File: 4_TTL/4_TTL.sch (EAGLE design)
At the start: 3 parts, among them J1 MA03-2W, X1 ALLSERIALD, X2 AKL18X-10W

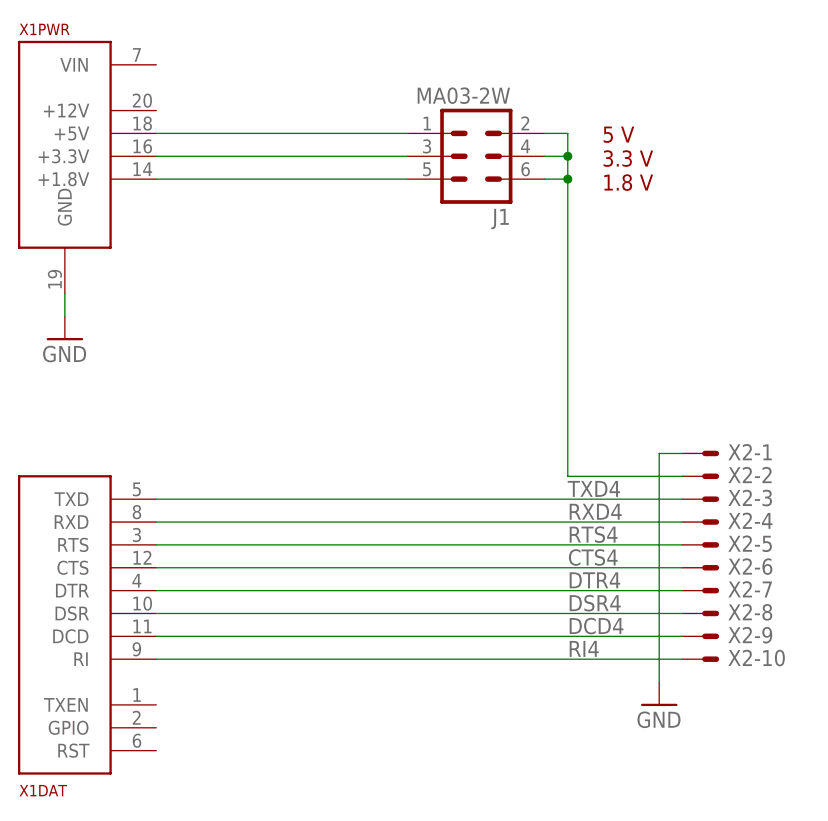
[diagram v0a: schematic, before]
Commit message: insert diode for supply
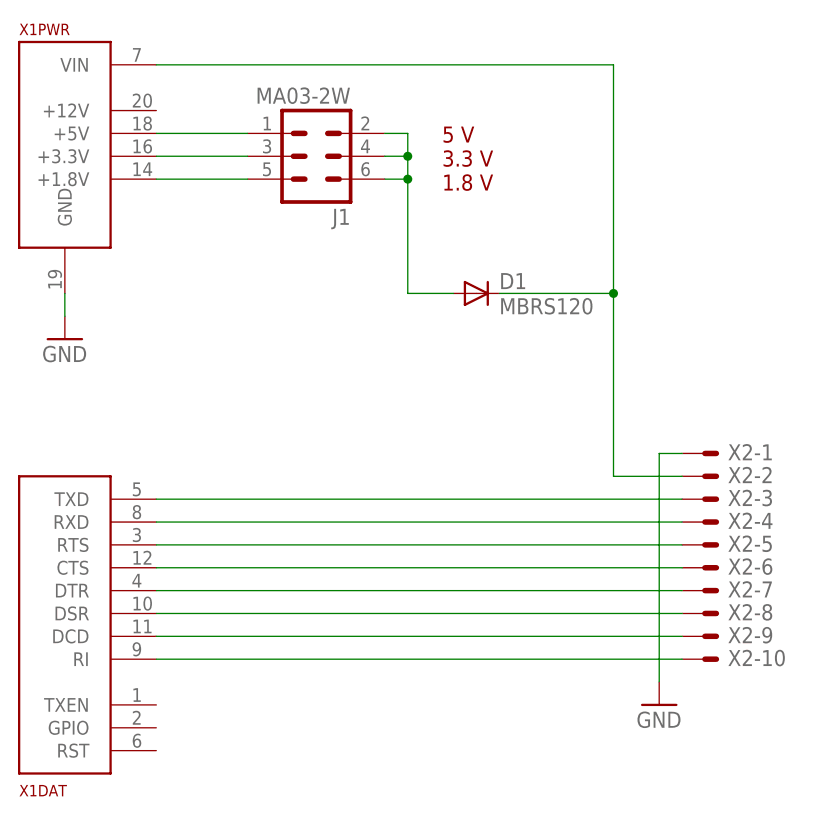
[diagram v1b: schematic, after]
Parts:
- added D1: MBRS120, diode:DIODE-DO214AA
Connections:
- new net N$5: D1.C, X1PWR.VIN, X2-2.S
- net N$1: now also D1.A; no longer X2-2.S
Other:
- moved on the sheet: J1
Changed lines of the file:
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@@
 <?xml version="1.0" encoding="utf-8"?>
 <!DOCTYPE eagle SYSTEM "eagle.dtd">
-<eagle version="7.7.0">
+<eagle version="7.6.0">
 <drawing>
 <settings>
@@
 <part name="GND2" library="supply1" deviceset="GND" device=""/>
 <part name="J1" library="con-lstb" deviceset="MA03-2W" device=""/>
+<part name="D1" library="diode" deviceset="DIODE-" device="DO214AA" value="MBRS120"/>
 </parts>
 <sheets>
 <sheet>
 <plain>
-<text x="105.41" y="115.57" size="1.778" layer="94">5 V
+<text x="87.63" y="115.57" size="1.778" layer="94">5 V
 3.3 V
 1.8 V</text>
@@
 <instance part="GND1" gate="1" x="45.72" y="99.06"/>
 <instance part="GND2" gate="1" x="111.76" y="58.42"/>
-<instance part="J1" gate="G$1" x="91.44" y="119.38" rot="R180"/>
+<instance part="J1" gate="G$1" x="73.66" y="119.38" rot="R180"/>
+<instance part="D1" gate="G$1" x="91.44" y="104.14"/>
 </instances>
 <busses>
@@
 <segment>
 <pinref part="X2" gate="-3" pin="S"/>
-<label x="101.6" y="81.534" size="1.778" layer="95"/>
 <pinref part="X1" gate="DAT" pin="TXD"/>
 <wire x1="114.3" y1="81.28" x2="55.88" y2="81.28" width="0.1524" layer="91"/>
@@
 <segment>
 <pinref part="X2" gate="-4" pin="S"/>
-<label x="101.6" y="78.994" size="1.778" layer="95"/>
 <pinref part="X1" gate="DAT" pin="RXD"/>
 <wire x1="114.3" y1="78.74" x2="55.88" y2="78.74" width="0.1524" layer="91"/>
@@
 <segment>
 <pinref part="X2" gate="-5" pin="S"/>
-<label x="101.6" y="76.454" size="1.778" layer="95"/>
 <pinref part="X1" gate="DAT" pin="RTS"/>
 <wire x1="55.88" y1="76.2" x2="114.3" y2="76.2" width="0.1524" layer="91"/>
@@
 <segment>
 <pinref part="X2" gate="-6" pin="S"/>
-<label x="101.6" y="73.914" size="1.778" layer="95"/>
 <pinref part="X1" gate="DAT" pin="CTS"/>
 <wire x1="114.3" y1="73.66" x2="55.88" y2="73.66" width="0.1524" layer="91"/>
@@
 <segment>
 <pinref part="X2" gate="-7" pin="S"/>
-<label x="101.6" y="71.374" size="1.778" layer="95"/>
 <pinref part="X1" gate="DAT" pin="DTR"/>
 <wire x1="114.3" y1="71.12" x2="55.88" y2="71.12" width="0.1524" layer="91"/>
@@
 <segment>
 <pinref part="X2" gate="-8" pin="S"/>
-<label x="101.6" y="68.834" size="1.778" layer="95"/>
 <pinref part="X1" gate="DAT" pin="DSR"/>
 <wire x1="114.3" y1="68.58" x2="55.88" y2="68.58" width="0.1524" layer="91"/>
@@
 <segment>
 <pinref part="X2" gate="-9" pin="S"/>
-<label x="101.6" y="66.294" size="1.778" layer="95"/>
 <pinref part="X1" gate="DAT" pin="DCD"/>
 <wire x1="55.88" y1="66.04" x2="114.3" y2="66.04" width="0.1524" layer="91"/>
@@
 <segment>
 <pinref part="X2" gate="-10" pin="S"/>
-<label x="101.6" y="63.754" size="1.778" layer="95"/>
 <pinref part="X1" gate="DAT" pin="RI"/>
 <wire x1="114.3" y1="63.5" x2="55.88" y2="63.5" width="0.1524" layer="91"/>
@@
 <net name="N$1" class="0">
 <segment>
-<pinref part="X2" gate="-2" pin="S"/>
-<wire x1="114.3" y1="83.82" x2="101.6" y2="83.82" width="0.1524" layer="91"/>
-<wire x1="101.6" y1="83.82" x2="101.6" y2="116.84" width="0.1524" layer="91"/>
 <pinref part="J1" gate="G$1" pin="2"/>
-<wire x1="101.6" y1="116.84" x2="101.6" y2="119.38" width="0.1524" layer="91"/>
-<wire x1="101.6" y1="119.38" x2="101.6" y2="121.92" width="0.1524" layer="91"/>
-<wire x1="101.6" y1="121.92" x2="99.06" y2="121.92" width="0.1524" layer="91"/>
+<wire x1="83.82" y1="116.84" x2="83.82" y2="119.38" width="0.1524" layer="91"/>
+<wire x1="83.82" y1="119.38" x2="83.82" y2="121.92" width="0.1524" layer="91"/>
+<wire x1="83.82" y1="121.92" x2="81.28" y2="121.92" width="0.1524" layer="91"/>
 <pinref part="J1" gate="G$1" pin="4"/>
-<wire x1="99.06" y1="119.38" x2="101.6" y2="119.38" width="0.1524" layer="91"/>
-<junction x="101.6" y="119.38"/>
+<wire x1="81.28" y1="119.38" x2="83.82" y2="119.38" width="0.1524" layer="91"/>
+<junction x="83.82" y="119.38"/>
 <pinref part="J1" gate="G$1" pin="6"/>
-<wire x1="99.06" y1="116.84" x2="101.6" y2="116.84" width="0.1524" layer="91"/>
-<junction x="101.6" y="116.84"/>
+<wire x1="81.28" y1="116.84" x2="83.82" y2="116.84" width="0.1524" layer="91"/>
+<pinref part="D1" gate="G$1" pin="A"/>
+<wire x1="88.9" y1="104.14" x2="83.82" y2="104.14" width="0.1524" layer="91"/>
+<wire x1="83.82" y1="104.14" x2="83.82" y2="116.84" width="0.1524" layer="91"/>
+<junction x="83.82" y="116.84"/>
 </segment>
 </net>
@@
 <pinref part="X1" gate="PWR" pin="+1.8V"/>
 <pinref part="J1" gate="G$1" pin="5"/>
-<wire x1="55.88" y1="116.84" x2="83.82" y2="116.84" width="0.1524" layer="91"/>
+<wire x1="55.88" y1="116.84" x2="66.04" y2="116.84" width="0.1524" layer="91"/>
 </segment>
 </net>
@@
 <pinref part="X1" gate="PWR" pin="+3.3V"/>
 <pinref part="J1" gate="G$1" pin="3"/>
-<wire x1="55.88" y1="119.38" x2="83.82" y2="119.38" width="0.1524" layer="91"/>
+<wire x1="55.88" y1="119.38" x2="66.04" y2="119.38" width="0.1524" layer="91"/>
 </segment>
 </net>
@@
 <pinref part="X1" gate="PWR" pin="+5V"/>
 <pinref part="J1" gate="G$1" pin="1"/>
-<wire x1="55.88" y1="121.92" x2="83.82" y2="121.92" width="0.1524" layer="91"/>
-</segment>
-</net>
+<wire x1="55.88" y1="121.92" x2="66.04" y2="121.92" width="0.1524" layer="91"/>
+</segment>
+</net>
+<net name="N$5" class="0">
+<segment>
+<pinref part="X2" gate="-2" pin="S"/>
+<wire x1="114.3" y1="83.82" x2="106.68" y2="83.82" width="0.1524" layer="91"/>
+<pinref part="X1" gate="PWR" pin="VIN"/>
+<wire x1="55.88" y1="129.54" x2="106.68" y2="129.54" width="0.1524" layer="91"/>
+<wire x1="106.68" y1="129.54" x2="106.68" y2="104.14" width="0.1524" layer="91"/>
+<pinref part="D1" gate="G$1" pin="C"/>
+<wire x1="106.68" y1="104.14" x2="106.68" y2="83.82" width="0.1524" layer="91"/>
+<wire x1="93.98" y1="104.14" x2="106.68" y2="104.14" width="0.1524" layer="91"/>
+<junction x="106.68" y="104.14"/>
+</segment>
+</net>

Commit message: new BOMs,
finish TTY board
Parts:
- D1: OC_REICHELT (none) -> MBRS120SMD
- J1: OC_REICHELT (none) -> MPE 088-2-006
- X1: OC_REICHELT (none) -> SL 2X10W 2,54
- X2: OC_REICHELT (none) -> AKL 182-10
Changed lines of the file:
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@@
 <parts>
 <part name="FRAME4" library="frames" deviceset="A4L-LOC" device=""/>
-<part name="X2" library="con-riacon_akl" deviceset="AKL18X-10" device="W"/>
-<part name="X1" library="AllSerial" deviceset="ALLSERIAL" device="D"/>
+<part name="X2" library="con-riacon_akl" deviceset="AKL18X-10" device="W">
+<attribute name="OC_REICHELT" value="AKL 182-10"/>
+</part>
+<part name="X1" library="AllSerial" deviceset="ALLSERIAL" device="D">
+<attribute name="OC_REICHELT" value="SL 2X10W 2,54"/>
+</part>
 <part name="GND1" library="supply1" deviceset="GND" device=""/>
 <part name="GND2" library="supply1" deviceset="GND" device=""/>
-<part name="J1" library="con-lstb" deviceset="MA03-2W" device=""/>
-<part name="D1" library="diode" deviceset="DIODE-" device="DO214AA" value="MBRS120"/>
+<part name="J1" library="con-lstb" deviceset="MA03-2W" device="">
+<attribute name="OC_REICHELT" value="MPE 088-2-006"/>
+</part>
+<part name="D1" library="diode" deviceset="DIODE-" device="DO214AA" value="MBRS120">
+<attribute name="OC_REICHELT" value="MBRS120SMD"/>
+</part>
 </parts>
 <sheets>
@@
 <instance part="X2" gate="-3" x="116.84" y="81.28"/>
 <instance part="X2" gate="-4" x="116.84" y="78.74"/>
-<instance part="X2" gate="-5" x="116.84" y="76.2"/>
+<instance part="X2" gate="-5" x="116.84" y="76.2">
+<attribute name="OC_REICHELT" x="116.84" y="76.2" size="1.778" layer="96" display="off"/>
+</instance>
 <instance part="X2" gate="-6" x="116.84" y="73.66"/>
 <instance part="X2" gate="-7" x="116.84" y="71.12"/>
@@
 <instance part="X2" gate="-9" x="116.84" y="66.04"/>
 <instance part="X2" gate="-10" x="116.84" y="63.5"/>
-<instance part="X1" gate="DAT" x="45.72" y="66.04"/>
+<instance part="X1" gate="DAT" x="45.72" y="66.04">
+<attribute name="OC_REICHELT" x="45.72" y="66.04" size="1.778" layer="96" display="off"/>
+</instance>
 <instance part="X1" gate="PWR" x="45.72" y="119.38"/>
 <instance part="GND1" gate="1" x="45.72" y="99.06"/>
 <instance part="GND2" gate="1" x="111.76" y="58.42"/>
-<instance part="J1" gate="G$1" x="73.66" y="119.38" rot="R180"/>
-<instance part="D1" gate="G$1" x="91.44" y="104.14"/>
+<instance part="J1" gate="G$1" x="73.66" y="119.38" rot="R180">
+<attribute name="OC_REICHELT" x="73.66" y="119.38" size="1.778" layer="96" rot="R180" display="off"/>
+</instance>
+<instance part="D1" gate="G$1" x="91.44" y="104.14">
+<attribute name="OC_REICHELT" x="91.44" y="104.14" size="1.778" layer="96" display="off"/>
+</instance>
 </instances>
 <busses>

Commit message: add author
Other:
- note added: "Seegel Systeme Königstraße 57 90762 Fürth www.seegel-systeme.de post@seegel-systeme.de +49 (911) / 8915295"
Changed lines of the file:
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@@
 <?xml version="1.0" encoding="utf-8"?>
 <!DOCTYPE eagle SYSTEM "eagle.dtd">
-<eagle version="7.6.0">
+<eagle version="7.7.0">
 <drawing>
 <settings>
@@
 3.3 V
 1.8 V</text>
+<text x="165.1" y="7.62" size="1.778" layer="94">Seegel Systeme
+Königstraße 57
+90762 Fürth
+www.seegel-systeme.de
+post@seegel-systeme.de
++49 (911) / 8915295</text>
 </plain>
 <instances>

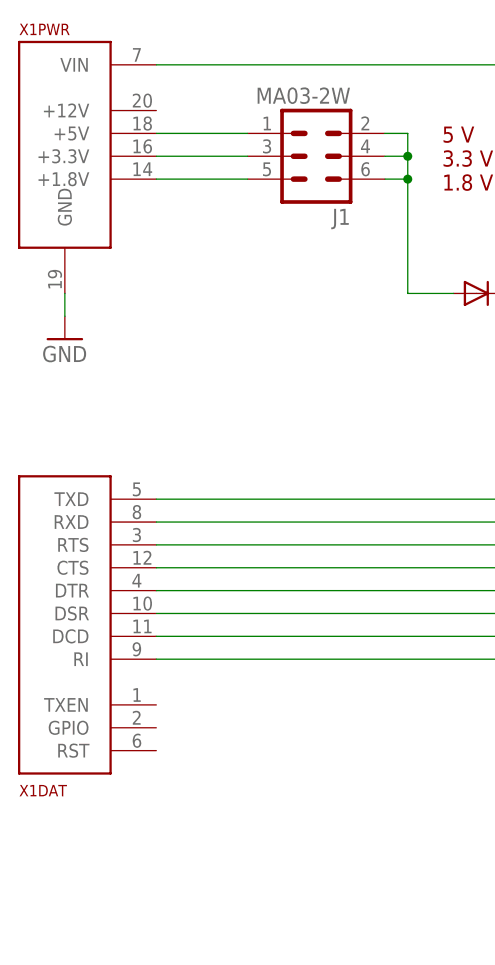
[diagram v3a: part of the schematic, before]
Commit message: change to libv2
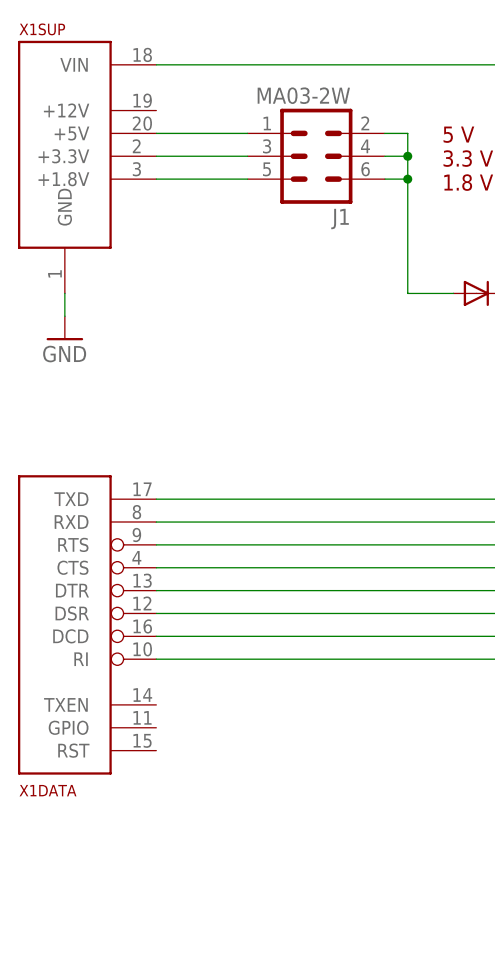
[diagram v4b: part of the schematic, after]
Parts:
- X1: value ALLSERIALD -> ALLSERIALSLAVE; device AllSerial:ALLSERIALD -> AllSerialv2:ALLSERIALSLAVE; OC_REICHELT SL 2X10W 2,54 -> (none)
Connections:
- net CTS4: now also X1DATA.CTS; no longer X1DAT.CTS
- net DCD4: now also X1DATA.DCD; no longer X1DAT.DCD
- net DSR4: now also X1DATA.DSR; no longer X1DAT.DSR
- net DTR4: now also X1DATA.DTR; no longer X1DAT.DTR
- net GND: now also X1SUP.GND; no longer X1PWR.GND
- net N$2: now also X1SUP.+1.8V; no longer X1PWR.+1.8V
- net N$3: now also X1SUP.+3.3V; no longer X1PWR.+3.3V
- net N$4: now also X1SUP.+5V; no longer X1PWR.+5V
- net N$5: now also X1SUP.VIN; no longer X1PWR.VIN
- net RI4: now also X1DATA.RI; no longer X1DAT.RI
- net RTS4: now also X1DATA.RTS; no longer X1DAT.RTS
- net RXD4: now also X1DATA.RXD; no longer X1DAT.RXD
- net TXD4: now also X1DATA.TXD; no longer X1DAT.TXD
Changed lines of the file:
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@@
 <?xml version="1.0" encoding="utf-8"?>
 <!DOCTYPE eagle SYSTEM "eagle.dtd">
-<eagle version="7.7.0">
+<eagle version="7.6.0">
 <drawing>
 <settings>
@@
 <attribute name="OC_REICHELT" value="AKL 182-10"/>
 </part>
-<part name="X1" library="AllSerial" deviceset="ALLSERIAL" device="D">
-<attribute name="OC_REICHELT" value="SL 2X10W 2,54"/>
-</part>
 <part name="GND1" library="supply1" deviceset="GND" device=""/>
 <part name="GND2" library="supply1" deviceset="GND" device=""/>
@@
 <attribute name="OC_REICHELT" value="MBRS120SMD"/>
 </part>
+<part name="X1" library="AllSerialv2" deviceset="ALLSERIALSLAVE" device=""/>
 </parts>
 <sheets>
@@
 <instance part="X2" gate="-9" x="116.84" y="66.04"/>
 <instance part="X2" gate="-10" x="116.84" y="63.5"/>
-<instance part="X1" gate="DAT" x="45.72" y="66.04">
-<attribute name="OC_REICHELT" x="45.72" y="66.04" size="1.778" layer="96" display="off"/>
-</instance>
-<instance part="X1" gate="PWR" x="45.72" y="119.38"/>
 <instance part="GND1" gate="1" x="45.72" y="99.06"/>
 <instance part="GND2" gate="1" x="111.76" y="58.42"/>
@@
 <attribute name="OC_REICHELT" x="91.44" y="104.14" size="1.778" layer="96" display="off"/>
 </instance>
+<instance part="X1" gate="DATA" x="45.72" y="66.04"/>
+<instance part="X1" gate="SUP" x="45.72" y="119.38"/>
 </instances>
 <busses>
@@
 <segment>
 <pinref part="X2" gate="-3" pin="S"/>
-<pinref part="X1" gate="DAT" pin="TXD"/>
 <wire x1="114.3" y1="81.28" x2="55.88" y2="81.28" width="0.1524" layer="91"/>
+<pinref part="X1" gate="DATA" pin="TXD"/>
 </segment>
 </net>
@@
 <segment>
 <pinref part="X2" gate="-4" pin="S"/>
-<pinref part="X1" gate="DAT" pin="RXD"/>
 <wire x1="114.3" y1="78.74" x2="55.88" y2="78.74" width="0.1524" layer="91"/>
+<pinref part="X1" gate="DATA" pin="RXD"/>
 </segment>
 </net>
@@
 <segment>
 <pinref part="X2" gate="-5" pin="S"/>
-<pinref part="X1" gate="DAT" pin="RTS"/>
 <wire x1="55.88" y1="76.2" x2="114.3" y2="76.2" width="0.1524" layer="91"/>
+<pinref part="X1" gate="DATA" pin="RTS"/>
 </segment>
 </net>
@@
 <segment>
 <pinref part="X2" gate="-6" pin="S"/>
-<pinref part="X1" gate="DAT" pin="CTS"/>
 <wire x1="114.3" y1="73.66" x2="55.88" y2="73.66" width="0.1524" layer="91"/>
+<pinref part="X1" gate="DATA" pin="CTS"/>
 </segment>
 </net>
@@
 <segment>
 <pinref part="X2" gate="-7" pin="S"/>
-<pinref part="X1" gate="DAT" pin="DTR"/>
 <wire x1="114.3" y1="71.12" x2="55.88" y2="71.12" width="0.1524" layer="91"/>
+<pinref part="X1" gate="DATA" pin="DTR"/>
 </segment>
 </net>
@@
 <segment>
 <pinref part="X2" gate="-8" pin="S"/>
-<pinref part="X1" gate="DAT" pin="DSR"/>
 <wire x1="114.3" y1="68.58" x2="55.88" y2="68.58" width="0.1524" layer="91"/>
+<pinref part="X1" gate="DATA" pin="DSR"/>
 </segment>
 </net>
@@
 <segment>
 <pinref part="X2" gate="-9" pin="S"/>
-<pinref part="X1" gate="DAT" pin="DCD"/>
 <wire x1="55.88" y1="66.04" x2="114.3" y2="66.04" width="0.1524" layer="91"/>
+<pinref part="X1" gate="DATA" pin="DCD"/>
 </segment>
 </net>
@@
 <segment>
 <pinref part="X2" gate="-10" pin="S"/>
-<pinref part="X1" gate="DAT" pin="RI"/>
 <wire x1="114.3" y1="63.5" x2="55.88" y2="63.5" width="0.1524" layer="91"/>
+<pinref part="X1" gate="DATA" pin="RI"/>
 </segment>
 </net>
 <net name="GND" class="0">
 <segment>
-<pinref part="X1" gate="PWR" pin="GND"/>
 <wire x1="45.72" y1="101.6" x2="45.72" y2="104.14" width="0.1524" layer="91"/>
 <pinref part="GND1" gate="1" pin="GND"/>
+<pinref part="X1" gate="SUP" pin="GND"/>
 </segment>
 <segment>
@@
 <net name="N$2" class="0">
 <segment>
-<pinref part="X1" gate="PWR" pin="+1.8V"/>
 <pinref part="J1" gate="G$1" pin="5"/>
 <wire x1="55.88" y1="116.84" x2="66.04" y2="116.84" width="0.1524" layer="91"/>
+<pinref part="X1" gate="SUP" pin="+1.8V"/>
 </segment>
 </net>
 <net name="N$3" class="0">
 <segment>
-<pinref part="X1" gate="PWR" pin="+3.3V"/>
 <pinref part="J1" gate="G$1" pin="3"/>
 <wire x1="55.88" y1="119.38" x2="66.04" y2="119.38" width="0.1524" layer="91"/>
+<pinref part="X1" gate="SUP" pin="+3.3V"/>
 </segment>
 </net>
 <net name="N$4" class="0">
 <segment>
-<pinref part="X1" gate="PWR" pin="+5V"/>
 <pinref part="J1" gate="G$1" pin="1"/>
 <wire x1="55.88" y1="121.92" x2="66.04" y2="121.92" width="0.1524" layer="91"/>
+<pinref part="X1" gate="SUP" pin="+5V"/>
 </segment>
 </net>
@@
 <pinref part="X2" gate="-2" pin="S"/>
 <wire x1="114.3" y1="83.82" x2="106.68" y2="83.82" width="0.1524" layer="91"/>
-<pinref part="X1" gate="PWR" pin="VIN"/>
 <wire x1="55.88" y1="129.54" x2="106.68" y2="129.54" width="0.1524" layer="91"/>
 <wire x1="106.68" y1="129.54" x2="106.68" y2="104.14" width="0.1524" layer="91"/>
@@
 <wire x1="93.98" y1="104.14" x2="106.68" y2="104.14" width="0.1524" layer="91"/>
 <junction x="106.68" y="104.14"/>
-</segment>
-</net>
+<pinref part="X1" gate="SUP" pin="VIN"/>
+</segment>
+</net>

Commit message: final design & order
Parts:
- removed D1: MBRS120, diode:DIODE-DO214AA
- removed J1: MA03-2W, con-lstb:MA03-2W
- added C1, C2: 1µ, rcl:C-EUC0805K
- added IC1: MCP1700T-2502E, SeeSys:MCP170X
- added SV1: X3, con-lstb:MA04-2W
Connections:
- removed net N$3: J1.3, X1SUP.+3.3V
- new net N$6: C2.1, IC1.OUT, SV1.5
- net GND: now also C1.2, C2.2, IC1.GND
- net N$1: now also SV1.2, SV1.4, SV1.6, SV1.8, X1SUP.VIN, X2-2.S; no longer D1.A, J1.2, J1.4, J1.6
- net N$2: now also SV1.7; no longer J1.5
- net N$4: now also SV1.1; no longer J1.1
- net N$5: now also C1.1, IC1.IN, SV1.3, X1SUP.+3.3V; no longer D1.C, X1SUP.VIN, X2-2.S
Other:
- note added: "5 V 3.3 V 2.5 V 1.8 V"
- note removed: "5 V 3.3 V 1.8 V"
- moved on the sheet: X2-1, X2-10, X2-2, X2-3, X2-4, X2-5, X2-6, X2-7, X2-8, X2-9
